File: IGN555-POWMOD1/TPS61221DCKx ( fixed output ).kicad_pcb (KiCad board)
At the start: 2 copper layers, 21 x 21 mm, 6 parts, among them J1 Conn_01x02_Pin, U1 TPS61221DCK

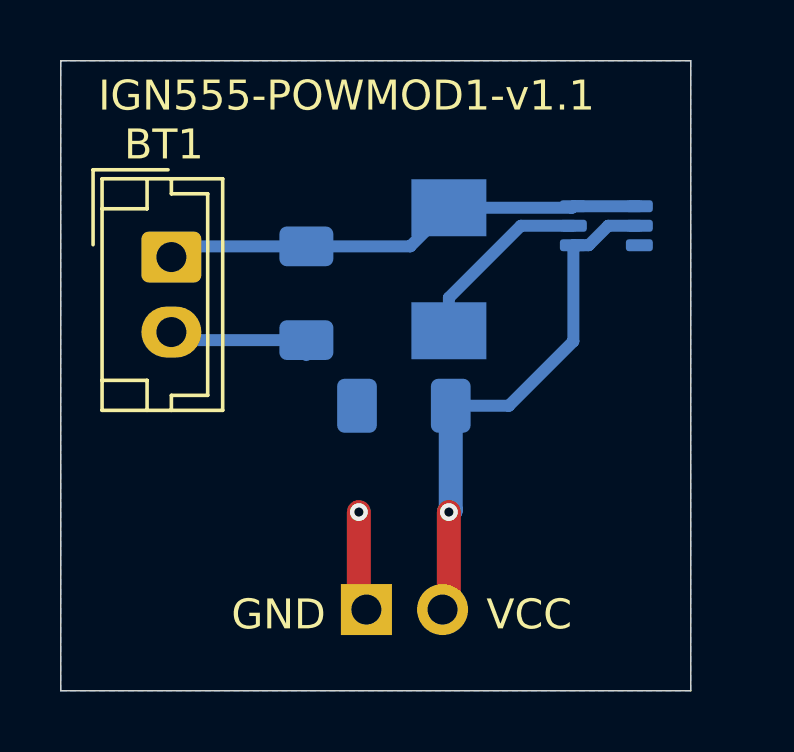
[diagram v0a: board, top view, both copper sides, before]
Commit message: Move path out of the inductance zone
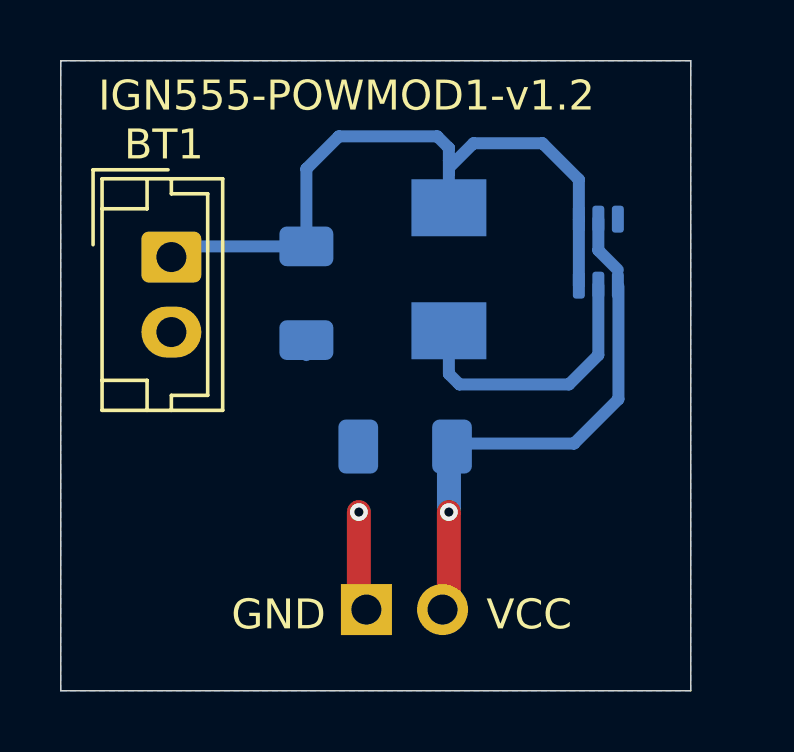
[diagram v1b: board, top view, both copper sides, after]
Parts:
- moved C1 1.36 mm to (148.2, 106.4)
- moved U1 0.92 mm to (154.7, 99.9), turned to -90 degrees
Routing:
- net Vbat: track 16.3 -> 23.3 mm
- net GND: track 8.55 -> 4.26 mm
- net Net-(U1-L): track 6.24 -> 9.30 mm
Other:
- board text added: "IGN555-POWMOD1-v1.2"
- board text removed: "IGN555-POWMOD1-v1.1"
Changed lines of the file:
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@@
 		)
 		(property "Value" "Battery_Cell"
-			(at 6.75 -1.5 180)
+			(at 9.74625 1.6075 90)
 			(layer "F.Fab")
 			(effects
@@
 	(footprint "Package_TO_SOT_SMD:Texas_R-PDSO-G6"
 		(layer "B.Cu")
-		(at 154.9375 99 180)
+		(at 154.67 99.88 -90)
 		(descr "R-PDSO-G6, http://www.ti.com/lit/ds/slis144b/slis144b.pdf")
 		(tags "R-PDSO-G6 SC-70-6")
 		(property "Reference" "U1"
-			(at 0 3 0)
+			(at -2.854878 0.005 180)
 			(layer "B.SilkS")
 			(effects
@@
 		)
 		(property "Value" "TPS61221DCK"
-			(at 0 -4.29375 90)
+			(at 5.71 -1.95 90)
 			(layer "B.Fab")
 			(effects
@@
 		)
 		(property "Footprint" "Package_TO_SOT_SMD:Texas_R-PDSO-G6"
-			(at 0 0 0)
+			(at 0 0 90)
 			(unlocked yes)
 			(layer "B.Fab")
@@
 		)
 		(property "Datasheet" "http://www.ti.com/lit/ds/symlink/tps61220.pdf"
-			(at 0 0 0)
+			(at 0 0 90)
 			(unlocked yes)
 			(layer "B.Fab")
@@
 		)
 		(property "Description" "400 mA Step-Up Converter, Fixed 3.3V Output Voltage, 0.7-5.5V Input Voltage, SC-70"
-			(at 0 0 0)
+			(at 0 0 90)
 			(unlocked yes)
 			(layer "B.Fab")
@@
 		(fp_line
 			(start 1.6 1.4)
+			(end -1.6 1.4)
+			(stroke
+				(width 0.05)
+				(type solid)
+			)
+			(layer "B.CrtYd")
+		)
+		(fp_line
+			(start 1.6 1.4)
 			(end 1.6 -1.4)
 			(stroke
@@
 		)
 		(fp_line
-			(start 1.6 1.4)
+			(start -1.6 -1.4)
 			(end -1.6 1.4)
 			(stroke
@@
 		)
 		(fp_line
-			(start -1.6 -1.4)
-			(end -1.6 1.4)
-			(stroke
-				(width 0.05)
-				(type solid)
-			)
-			(layer "B.CrtYd")
+			(start -0.175 1.1)
+			(end 0.675 1.1)
+			(stroke
+				(width 0.1)
+				(type solid)
+			)
+			(layer "B.Fab")
+		)
+		(fp_line
+			(start -0.675 0.6)
+			(end -0.175 1.1)
+			(stroke
+				(width 0.1)
+				(type solid)
+			)
+			(layer "B.Fab")
+		)
+		(fp_line
+			(start -0.675 -1.1)
+			(end -0.675 0.6)
+			(stroke
+				(width 0.1)
+				(type solid)
+			)
+			(layer "B.Fab")
+		)
+		(fp_line
+			(start -0.675 -1.1)
+			(end 0.675 -1.1)
+			(stroke
+				(width 0.1)
+				(type solid)
+			)
+			(layer "B.Fab")
 		)
 		(fp_line
@@
 			(layer "B.Fab")
 		)
-		(fp_line
-			(start -0.175 1.1)
-			(end 0.675 1.1)
-			(stroke
-				(width 0.1)
-				(type solid)
-			)
-			(layer "B.Fab")
-		)
-		(fp_line
-			(start -0.675 0.6)
-			(end -0.175 1.1)
-			(stroke
-				(width 0.1)
-				(type solid)
-			)
-			(layer "B.Fab")
-		)
-		(fp_line
-			(start -0.675 -1.1)
-			(end 0.675 -1.1)
-			(stroke
-				(width 0.1)
-				(type solid)
-			)
-			(layer "B.Fab")
-		)
-		(fp_line
-			(start -0.675 -1.1)
-			(end -0.675 0.6)
-			(stroke
-				(width 0.1)
-				(type solid)
-			)
-			(layer "B.Fab")
-		)
 		(fp_text user "${REFERENCE}"
-			(at 0 0 90)
+			(at 0 0 360)
 			(layer "B.Fab")
 			(effects
@@
 		)
 		(pad "1" smd roundrect
-			(at -1.1 0.65 180)
+			(at -1.1 0.65 270)
 			(size 0.9 0.4)
 			(layers "B.Cu" "B.Paste" "B.Mask")
@@
 		)
 		(pad "2" smd roundrect
-			(at -1.1 0 180)
+			(at -1.1 0 270)
 			(size 0.9 0.4)
 			(layers "B.Cu" "B.Paste" "B.Mask")
@@
 		)
 		(pad "3" smd roundrect
-			(at -1.1 -0.65 180)
+			(at -1.1 -0.65 270)
 			(size 0.9 0.4)
 			(layers "B.Cu" "B.Paste" "B.Mask")
@@
 		)
 		(pad "4" smd roundrect
-			(at 1.1 -0.65 180)
+			(at 1.1 -0.65 270)
 			(size 0.9 0.4)
 			(layers "B.Cu" "B.Paste" "B.Mask")
@@
 		)
 		(pad "5" smd roundrect
-			(at 1.1 0 180)
+			(at 1.1 0 270)
 			(size 0.9 0.4)
 			(layers "B.Cu" "B.Paste" "B.Mask")
@@
 		)
 		(pad "6" smd roundrect
-			(at 1.1 0.65 180)
+			(at 1.1 0.65 270)
 			(size 0.9 0.4)
 			(layers "B.Cu" "B.Paste" "B.Mask")
@@
 	(footprint "Capacitor_SMD:C_1206_3216Metric_Pad1.33x1.80mm_HandSolder"
 		(layer "B.Cu")
-		(at 148.1875 105 180)
+		(at 148.23 106.36 180)
 		(descr "Capacitor SMD 1206 (3216 Metric), square (rectangular) end terminal, IPC_7351 nominal with elongated pad for handsoldering. (Body size source: IPC-SM-782 page 76, https://www.pcb-3d.com/wordpress/wp-content/uploads/ipc-sm-782a_amendment_1_and_2.pdf), generated with kicad-footprint-generator")
 		(tags "capacitor handsolder")
@@
 		(tags "Inductor bmrx mchi")
 		(property "Reference" "L1"
-			(at 0.05 0 90)
+			(at -3.95 1.8575 180)
 			(layer "B.SilkS")
 			(effects
@@
 		(layer "Edge.Cuts")
 	)
-	(gr_text "IGN555-POWMOD1-v1.1\n"
+	(gr_text "IGN555-POWMOD1-v1.2\n"
 		(at 138 95.25 0)
 		(layer "F.SilkS")
@@
 	)
 	(segment
-		(start 146.6875 104.9375)
-		(end 146.625 105)
+		(start 146.6875 106.34)
+		(end 146.6675 106.36)
 		(width 0.4)
 		(layer "B.Cu")
@@
 		(start 144.9375 102.8125)
 		(end 144.9375 103.3125)
-		(width 0.4)
-		(layer "B.Cu")
-		(net 1)
-	)
-	(segment
-		(start 144.9375 102.8125)
-		(end 140.70625 102.8125)
 		(width 0.4)
 		(layer "B.Cu")
@@
 	)
 	(segment
-		(start 153.8375 102.85)
-		(end 151.6875 105)
+		(start 155.34 104.78)
+		(end 153.86 106.26)
 		(width 0.4)
 		(layer "B.Cu")
@@
 	)
 	(segment
-		(start 154.347378 99.65)
-		(end 154.997378 99)
+		(start 154.67 99.820122)
+		(end 154.67 98.78)
 		(width 0.4)
 		(layer "B.Cu")
@@
 	)
 	(segment
-		(start 153.8375 99.65)
-		(end 154.347378 99.65)
-		(width 0.4)
+		(start 149.69 106.4625)
+		(end 149.69 108.54125)
+		(width 0.8)
 		(layer "B.Cu")
 		(net 2)
 	)
 	(segment
-		(start 154.997378 99)
-		(end 156.0375 99)
+		(start 155.32 100.470122)
+		(end 154.67 99.820122)
 		(width 0.4)
 		(layer "B.Cu")
@@
 	)
 	(segment
-		(start 149.75 108.48125)
+		(start 149.8925 106.26)
+		(end 149.7925 106.36)
+		(width 0.4)
+		(layer "B.Cu")
+		(net 2)
+	)
+	(segment
+		(start 155.34 101.02)
+		(end 155.34 104.78)
+		(width 0.4)
+		(layer "B.Cu")
+		(net 2)
+	)
+	(segment
+		(start 149.69 108.54125)
 		(end 149.6875 108.54375)
 		(width 0.8)
@@
 	)
 	(segment
-		(start 149.75 105)
-		(end 149.75 108.48125)
+		(start 149.7925 106.36)
+		(end 149.69 106.4625)
 		(width 0.8)
 		(layer "B.Cu")
@@
 	)
 	(segment
-		(start 151.6875 105)
-		(end 149.75 105)
-		(width 0.4)
-		(layer "B.Cu")
-		(net 2)
-	)
-	(segment
-		(start 153.8375 99.65)
-		(end 153.8375 102.85)
+		(start 153.86 106.26)
+		(end 149.8925 106.26)
 		(width 0.4)
 		(layer "B.Cu")
@@
 	)
 	(segment
-		(start 153.7875 98.4)
-		(end 153.8375 98.35)
+		(start 152.81 96.25)
+		(end 150.5075 96.25)
 		(width 0.4)
 		(layer "B.Cu")
@@
 	)
 	(segment
-		(start 149.6875 98.4)
-		(end 153.7875 98.4)
+		(start 144.9375 99.6875)
+		(end 144.9375 97.1025)
 		(width 0.4)
 		(layer "B.Cu")
@@
 	)
 	(segment
-		(start 156.0375 98.35)
-		(end 153.8375 98.35)
+		(start 150.5075 96.25)
+		(end 149.6875 97.07)
+		(width 0.4)
+		(layer "B.Cu")
+		(net 3)
+	)
+	(segment
+		(start 154.02 97.46)
+		(end 152.81 96.25)
+		(width 0.4)
+		(layer "B.Cu")
+		(net 3)
+	)
+	(segment
+		(start 149.6875 96.82)
+		(end 149.6875 97.24)
+		(width 0.4)
+		(layer "B.Cu")
+		(net 3)
+	)
+	(segment
+		(start 149.6875 96.4125)
+		(end 149.6875 96.82)
+		(width 0.4)
+		(layer "B.Cu")
+		(net 3)
+	)
+	(segment
+		(start 144.9375 97.1025)
+		(end 146.02 96.02)
 		(width 0.4)
 		(layer "B.Cu")
@@
 	)
 	(segment
-		(start 144.9375 99.6875)
-		(end 148.4 99.6875)
+		(start 149.6875 97.24)
+		(end 149.6875 98.4)
 		(width 0.4)
 		(layer "B.Cu")
@@
 	)
 	(segment
-		(start 148.4 99.6875)
-		(end 149.6875 98.4)
+		(start 154.02 98.78)
+		(end 154.02 100.98)
 		(width 0.4)
 		(layer "B.Cu")
@@
 	)
 	(segment
-		(start 149.6875 101.4)
-		(end 149.6875 102.5)
+		(start 154.02 98.78)
+		(end 154.02 97.46)
+		(width 0.4)
+		(layer "B.Cu")
+		(net 3)
+	)
+	(segment
+		(start 149.3 96.02)
+		(end 149.69 96.41)
+		(width 0.4)
+		(layer "B.Cu")
+		(net 3)
+	)
+	(segment
+		(start 149.69 96.41)
+		(end 149.6875 96.4125)
+		(width 0.4)
+		(layer "B.Cu")
+		(net 3)
+	)
+	(segment
+		(start 146.02 96.02)
+		(end 149.3 96.02)
+		(width 0.4)
+		(layer "B.Cu")
+		(net 3)
+	)
+	(segment
+		(start 149.6875 102.5)
+		(end 149.6875 103.9375)
 		(width 0.4)
 		(layer "B.Cu")
@@
 	)
 	(segment
-		(start 152.0875 99)
-		(end 149.6875 101.4)
+		(start 153.69 104.29)
+		(end 154.67 103.31)
 		(width 0.4)
 		(layer "B.Cu")
@@
 	)
 	(segment
-		(start 153.8375 99)
-		(end 152.0875 99)
+		(start 154.67 103.31)
+		(end 154.67 100.98)
+		(width 0.4)
+		(layer "B.Cu")
+		(net 4)
+	)
+	(segment
+		(start 149.6875 103.9375)
+		(end 150.04 104.29)
+		(width 0.4)
+		(layer "B.Cu")
+		(net 4)
+	)
+	(segment
+		(start 150.04 104.29)
+		(end 153.69 104.29)
 		(width 0.4)
 		(layer "B.Cu")
@@
 		(hatch edge 0.5)
 		(connect_pads
-			(clearance 0.5)
+			(clearance 0.3)
 		)
 		(min_thickness 0.25)
